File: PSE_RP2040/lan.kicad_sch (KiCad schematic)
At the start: 32 parts, among them IC1 LAN8742A-CZ, T1 749013011, U4 USBLC6-4SC6

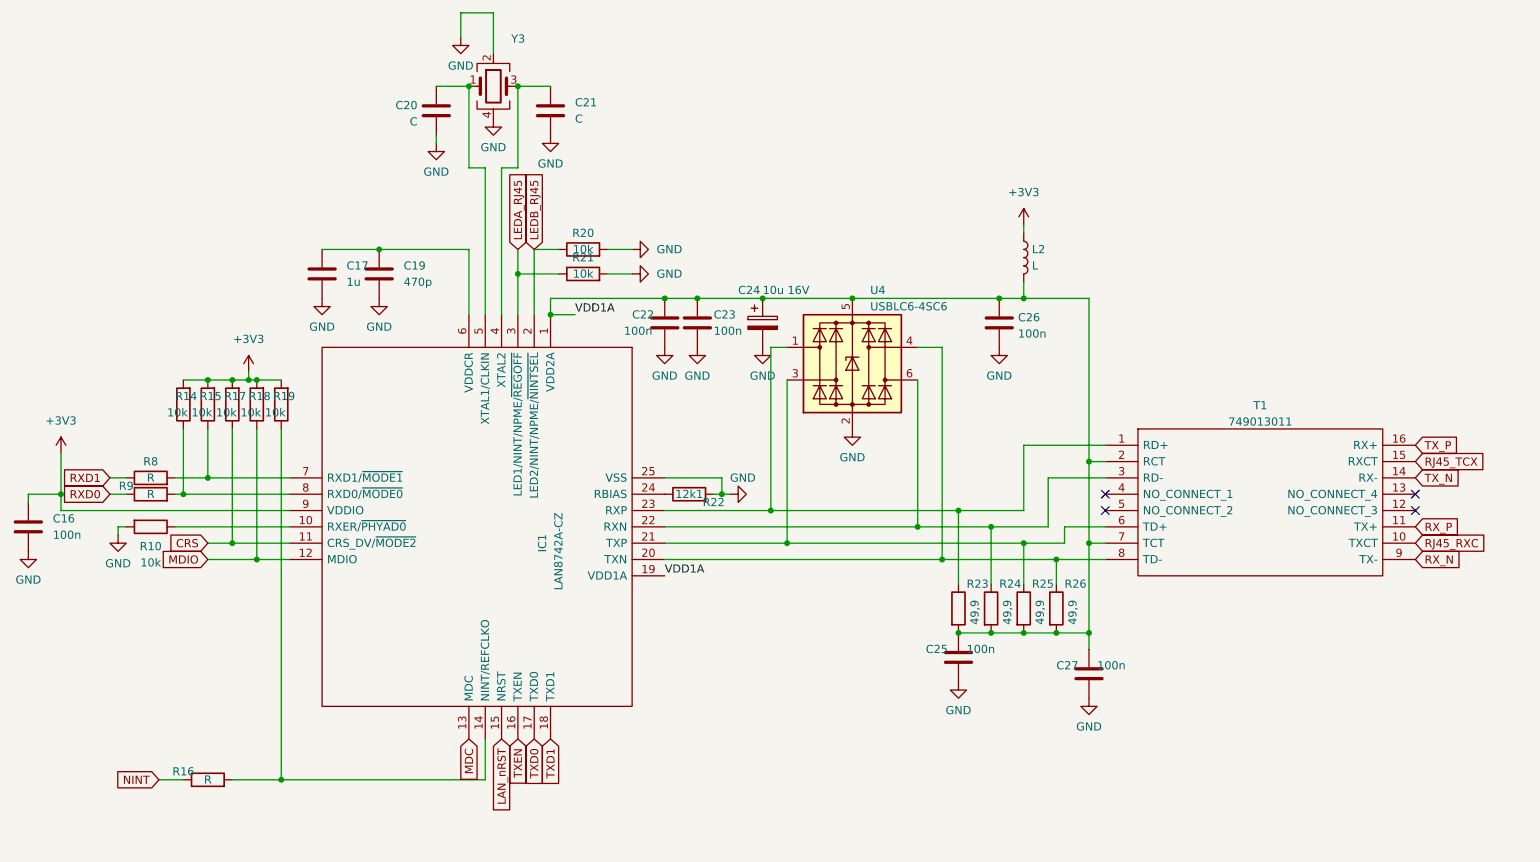
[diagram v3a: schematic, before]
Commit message: OR a diodi, connettore ext PoE
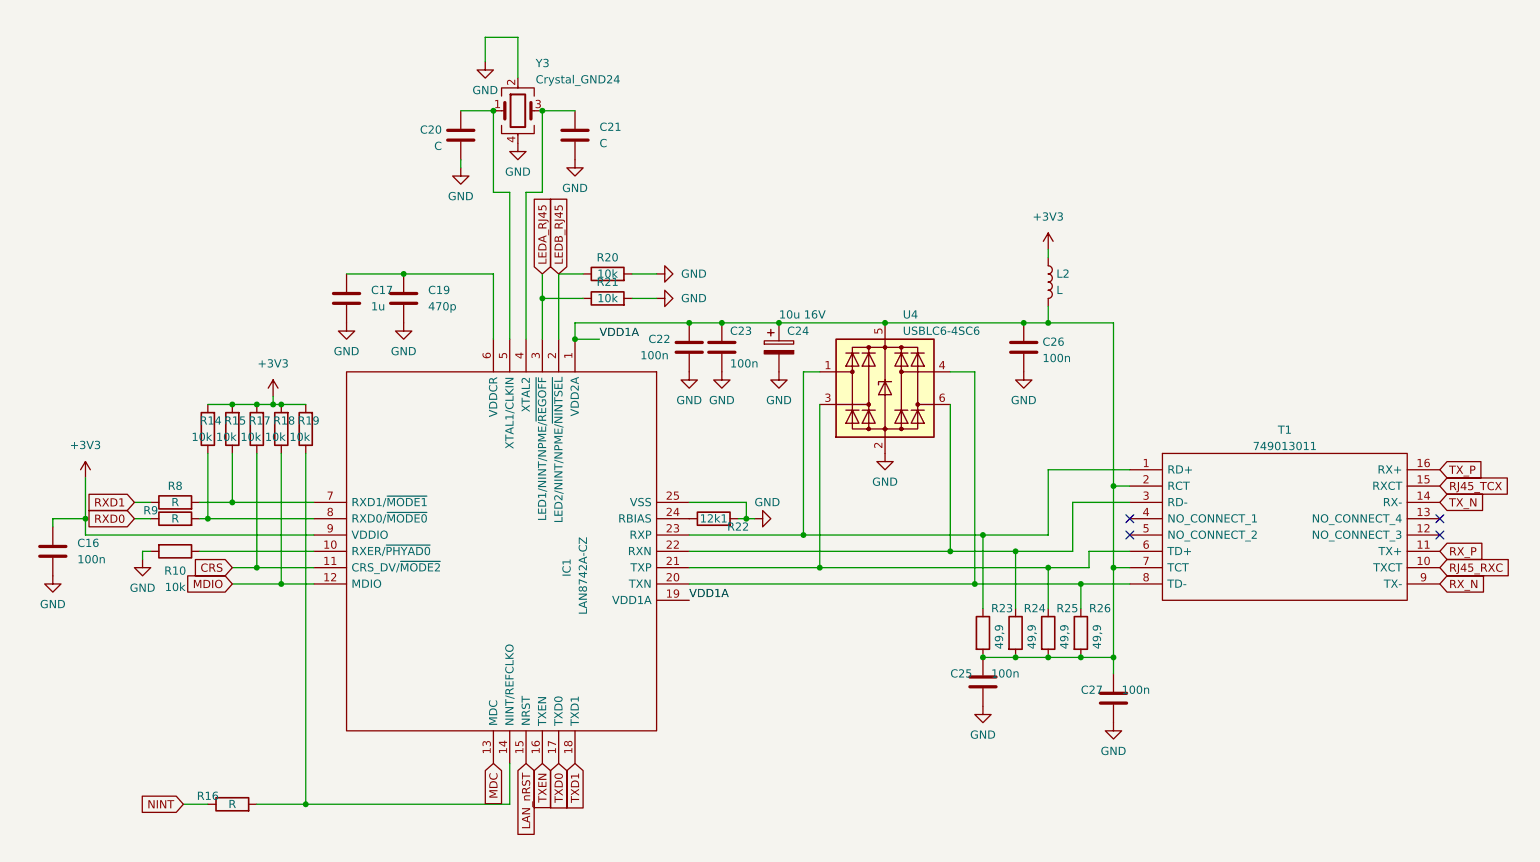
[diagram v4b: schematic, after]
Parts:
- C20, C21: footprint (none) -> Capacitor_SMD:C_0603_1608Metric
- Y3: value (none) -> Crystal_GND24; footprint (none) -> Crystal:Crystal_SMD_3225-4Pin_3.2x2.5mm_HandSoldering
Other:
- moved on the sheet: C16, C17, C19, C20, C21, C22, C23, C24, C25, C26, C27, IC1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

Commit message: valore resistenze lan
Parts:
- R16, R8, R9: value R -> (none)
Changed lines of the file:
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@@
     (in_bom yes) (on_board yes)
     (property "Reference" "R16" (id 0) (at 46.99 137.16 90))
-    (property "Value" "R" (id 1) (at 50.8 138.43 90))
+    (property "Value" "" (id 1) (at 50.8 138.43 90))
     (property "Footprint" "Resistor_SMD:R_0603_1608Metric" (id 2) (at 50.8 140.208 90)
       (effects (font (size 1.27 1.27)) hide)
@@
     (in_bom yes) (on_board yes)
     (property "Reference" "R9" (id 0) (at 38.1 92.71 90))
-    (property "Value" "R" (id 1) (at 41.91 93.98 90))
+    (property "Value" "" (id 1) (at 41.91 93.98 90))
     (property "Footprint" "Resistor_SMD:R_0603_1608Metric" (id 2) (at 41.91 95.758 90)
       (effects (font (size 1.27 1.27)) hide)
@@
     (in_bom yes) (on_board yes)
     (property "Reference" "R8" (id 0) (at 41.91 88.9 90))
-    (property "Value" "R" (id 1) (at 41.91 91.44 90))
+    (property "Value" "" (id 1) (at 41.91 91.44 90))
     (property "Footprint" "Resistor_SMD:R_0603_1608Metric" (id 2) (at 41.91 93.218 90)
       (effects (font (size 1.27 1.27)) hide)

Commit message: correzioni schema
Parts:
- C20, C21: value C -> (none)
- IC1: value LAN8742A-CZ -> (none)
- R16, R8, R9: value (none) -> 33
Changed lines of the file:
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@@
     (in_bom yes) (on_board yes)
     (property "Reference" "R16" (id 0) (at 46.99 137.16 90))
-    (property "Value" "" (id 1) (at 50.8 138.43 90))
+    (property "Value" "33" (id 1) (at 50.8 138.43 90))
     (property "Footprint" "Resistor_SMD:R_0603_1608Metric" (id 2) (at 50.8 140.208 90)
       (effects (font (size 1.27 1.27)) hide)
@@
     (in_bom yes) (on_board yes)
     (property "Reference" "R9" (id 0) (at 38.1 92.71 90))
-    (property "Value" "" (id 1) (at 41.91 93.98 90))
+    (property "Value" "33" (id 1) (at 41.91 93.98 90))
     (property "Footprint" "Resistor_SMD:R_0603_1608Metric" (id 2) (at 41.91 95.758 90)
       (effects (font (size 1.27 1.27)) hide)
@@
     (in_bom yes) (on_board yes)
     (property "Reference" "IC1" (id 0) (at 102.87 101.6 0))
-    (property "Value" "LAN8742A-CZ" (id 1) (at 105.41 102.87 0))
+    (property "Value" "" (id 1) (at 105.41 102.87 0))
     (property "Footprint" "" (id 2) (at 116.84 128.27 0)
       (effects (font (size 1.27 1.27)) (justify left) hide)
@@
   (symbol (lib_id "Device:C") (at 86.36 34.29 0) (unit 1)
     (in_bom yes) (on_board yes) (fields_autoplaced)
-    (property "Reference" "C20" (id 0) (at 83.439 33.4553 0)
-      (effects (font (size 1.27 1.27)) (justify right))
-    )
-    (property "Value" "C" (id 1) (at 83.439 35.9922 0)
-      (effects (font (size 1.27 1.27)) (justify right))
+    (property "Reference" "C20" (id 0) (at 90.17 33.0199 0)
+      (effects (font (size 1.27 1.27)) (justify left))
+    )
+    (property "Value" "" (id 1) (at 90.17 35.5599 0)
+      (effects (font (size 1.27 1.27)) (justify left))
     )
     (property "Footprint" "Capacitor_SMD:C_0603_1608Metric" (id 2) (at 87.3252 38.1 0)
@@
       (effects (font (size 1.27 1.27)) (justify left))
     )
-    (property "Value" "C" (id 1) (at 107.95 35.5599 0)
+    (property "Value" "" (id 1) (at 107.95 35.5599 0)
       (effects (font (size 1.27 1.27)) (justify left))
     )
@@
     (in_bom yes) (on_board yes)
     (property "Reference" "R8" (id 0) (at 41.91 88.9 90))
-    (property "Value" "" (id 1) (at 41.91 91.44 90))
+    (property "Value" "33" (id 1) (at 41.91 91.44 90))
     (property "Footprint" "Resistor_SMD:R_0603_1608Metric" (id 2) (at 41.91 93.218 90)
       (effects (font (size 1.27 1.27)) hide)

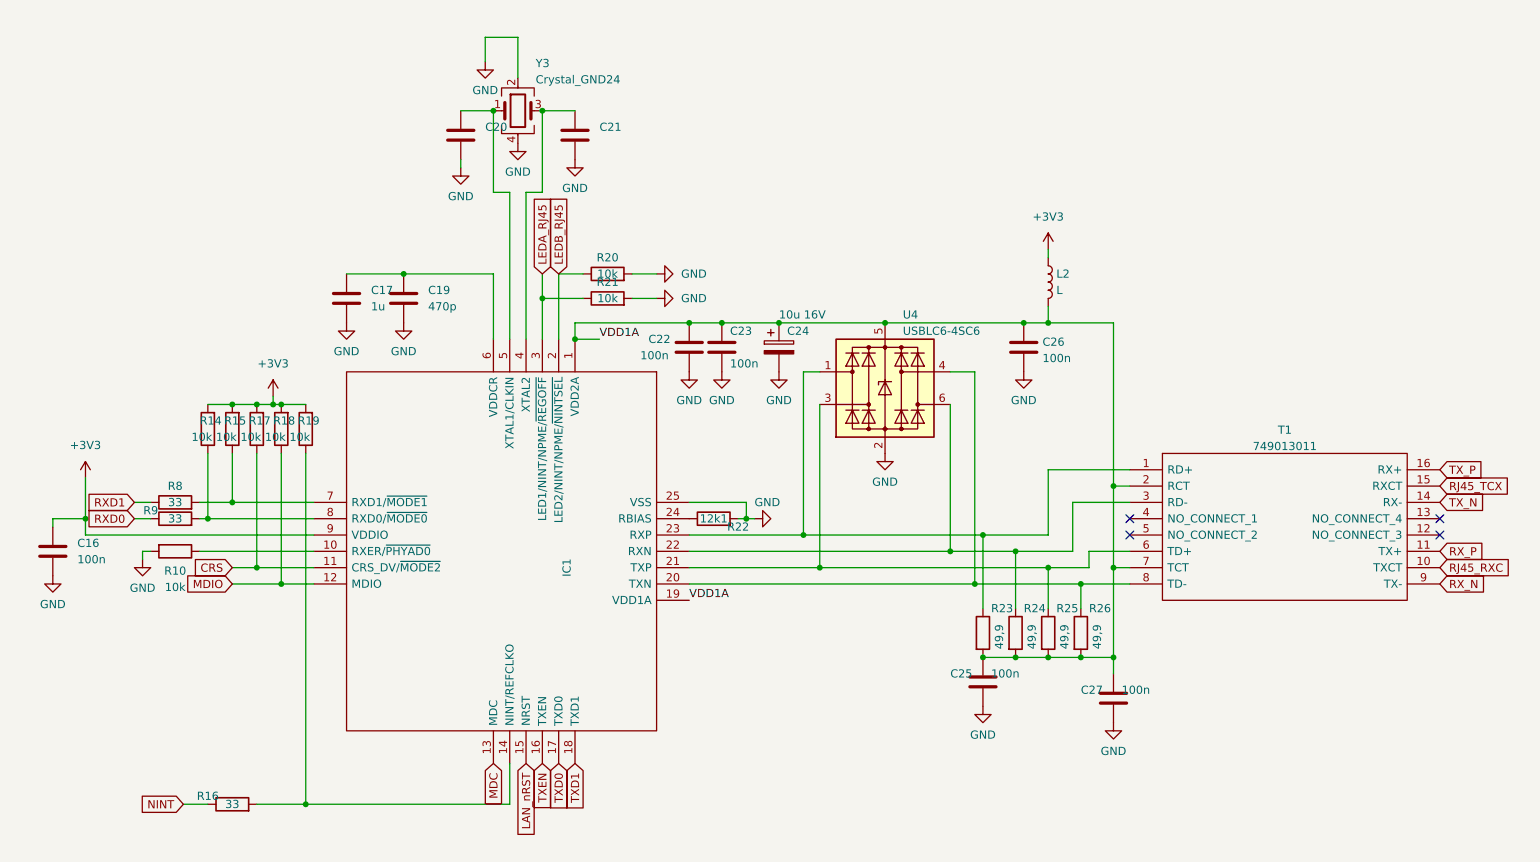
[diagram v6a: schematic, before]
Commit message: footprint, assegnamento
etichette (label)
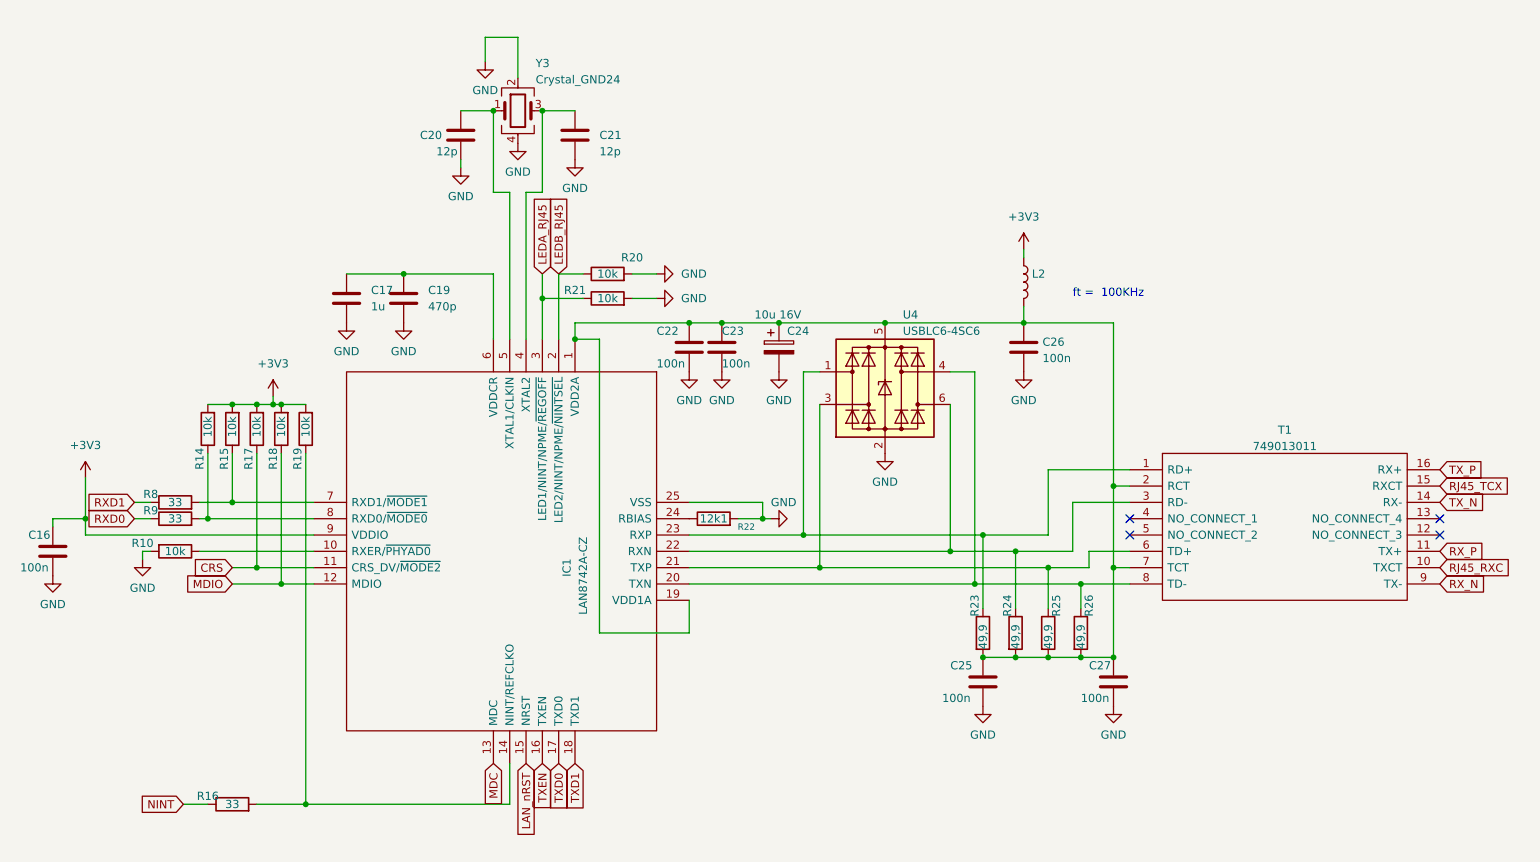
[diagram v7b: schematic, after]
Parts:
- C20, C21: value (none) -> 12p
- IC1: value (none) -> LAN8742A-CZ; footprint (none) -> Package_DFN_QFN:HVQFN-24-1EP_4x4mm_P0.5mm_EP2.5x2.5mm_ThermalVias
- L2: value L -> (none)
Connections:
- net VDD1A: no longer names the net of C22.1, C23.1, C24.1, C25.1, C26.1, C27.1, IC1.1 (VDD2A), IC1.19 (VDD1A), L2.2, R23.2, R24.2, R25.2, R26.2, T1.2 (RCT), T1.7 (TCT), U4.5 (VBUS)
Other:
- note added: "ft = 100KHz"
- moved on the sheet: C27, L2

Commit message: modifiche lezione
usb mini,
check s1b
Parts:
- L2: value (none) -> 25uH
- Y3: value Crystal_GND24 -> (none); footprint Crystal:Crystal_SMD_3225-4Pin_3.2x2.5mm_HandSoldering -> (none)
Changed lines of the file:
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@@
       (effects (font (size 1.27 1.27)) (justify left))
     )
-    (property "Value" "" (id 1) (at 175.26 58.4199 0)
+    (property "Value" "25uH" (id 1) (at 175.26 58.4199 0)
       (effects (font (size 1.27 1.27)) (justify left))
     )
@@
       (effects (font (size 1.27 1.27)) (justify left))
     )
-    (property "Value" "Crystal_GND24" (id 1) (at 98.0187 25.6341 0)
-      (effects (font (size 1.27 1.27)) (justify left))
-    )
-    (property "Footprint" "Crystal:Crystal_SMD_3225-4Pin_3.2x2.5mm_HandSoldering" (id 2) (at 95.25 30.48 0)
-      (effects (font (size 1.27 1.27)) hide)
-    )
+    (property "Value" "" (id 1) (at 98.0187 25.6341 0)
+      (effects (font (size 1.27 1.27)) (justify left))
+    )
+    (property "Footprint" "" (id 2) (at 95.25 30.48 0)
+      (effects (font (size 1.27 1.27)) hide)
+    )
